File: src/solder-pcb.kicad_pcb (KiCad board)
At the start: 2 copper layers, 99 x 82 mm, 44 parts, among them Q1 2N3904, Q10 2N3904, Q11 2N3904, Q12 2N3904, Q2 2N3904, Q3 2N3904, Q4 2N3904, Q5 2N3904, Q6 2N3904, Q7 2N3904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

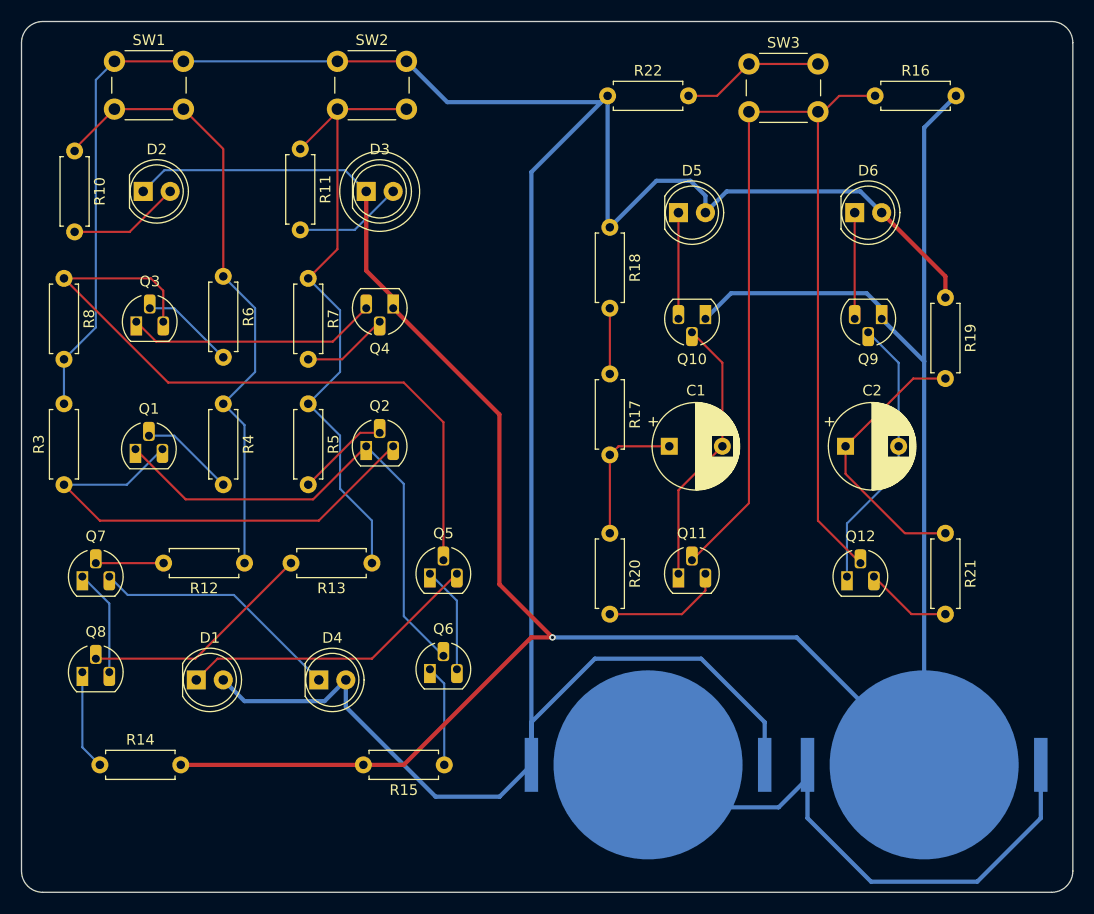
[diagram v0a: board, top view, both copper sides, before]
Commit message: Add some silkscreen diagrams
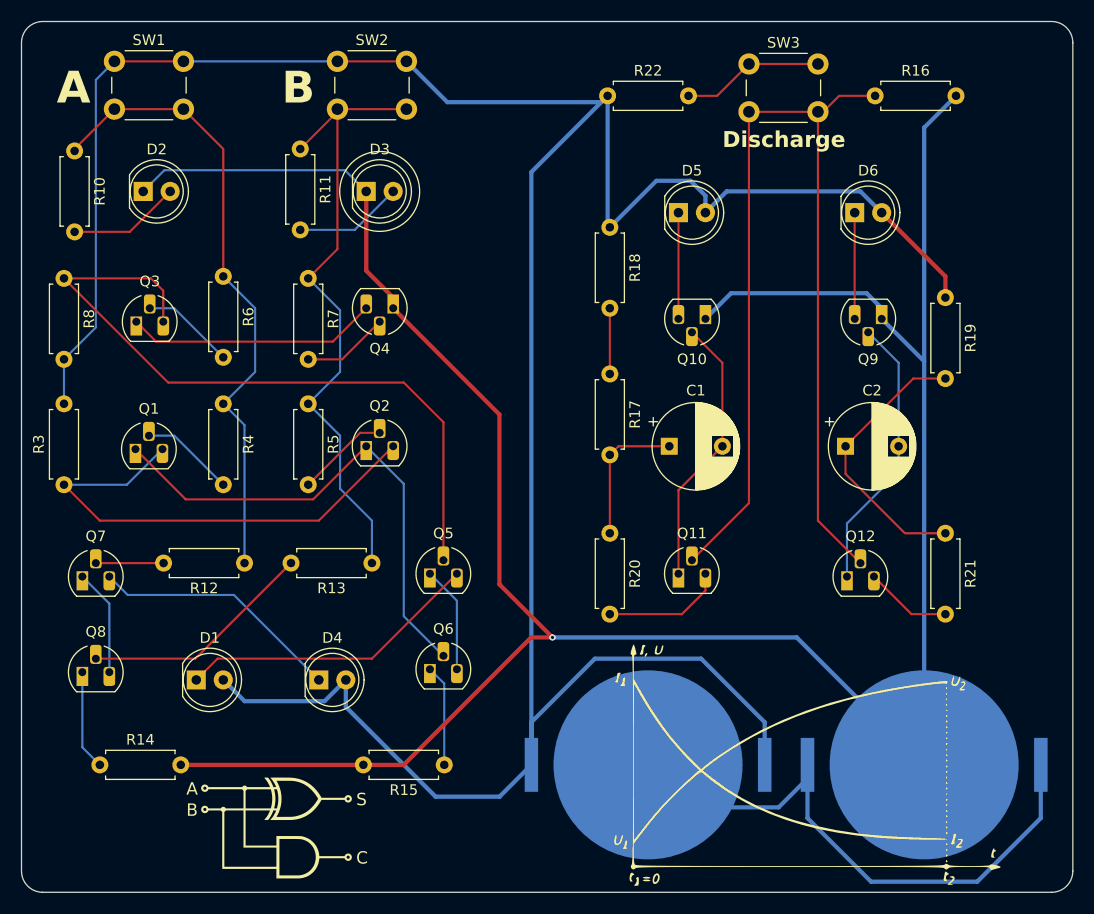
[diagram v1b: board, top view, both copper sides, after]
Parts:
- added G***: LOGO, LOGO, F.Cu at (169.0, 133.0)
- added G***: LOGO, LOGO, F.Cu at (119.0, 139.0)
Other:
- board text added: "A"
- board text added: "B"
- board text added: "Discharge"
